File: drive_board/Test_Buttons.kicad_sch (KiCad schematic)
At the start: 0 parts

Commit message: New Stuff
- Reverse voltage protection
- D-Pad for test buttons
- Rotary encoder for test buttons
- Finished ethernet circuit
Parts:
- added D2, D3, D4, D5: Orange, symbol Device:LED
- added R2, R3, R4, R5: 1k, Resistor_SMD:R_0603_1608Metric_Pad0.98x0.95mm_HandSolder, symbol Device:R_US
- added S1: 94HBB08T, CoreBoard:DIPS762W56P254L991H597Q6N, symbol CoreBoard:94HBB08T
- added SW1, SW2, SW3, SW4: SW_Push, Button_Switch_SMD:SW_SPST_TL3305A, symbol Switch:SW_Push
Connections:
- new net: D3.1 (K), R3.2
- new net: D2.1 (K), R2.2
- new net: D5.1 (K), R5.2
- new net: D4.1 (K), R4.2
- new net +3.3V: D2.2 (A), D3.2 (A), D4.2 (A), D5.2 (A), S1.2 (C_1), S1.5 (C_2)
- new net Back: R5.1, SW4.2
- new net Forward: R2.1, SW1.2
- new net GND: SW1.1, SW2.1, SW3.1, SW4.1
- new net Left: R3.1, SW2.2
- new net RTRY1: S1.1
- new net RTRY2: S1.4 (2)
- new net RTRY4: S1.3 (4)
- new net Right: R4.1, SW3.2
- no-connect marks 0 -> 1
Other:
- note added: "D-Pad"
- note added: "Rotary Encoder"

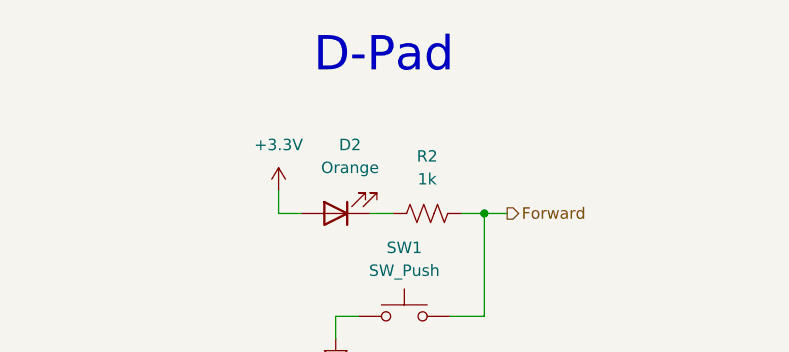
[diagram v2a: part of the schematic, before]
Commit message: More New Stuff
- Assigned pins on RoveNode
- Added some connectors
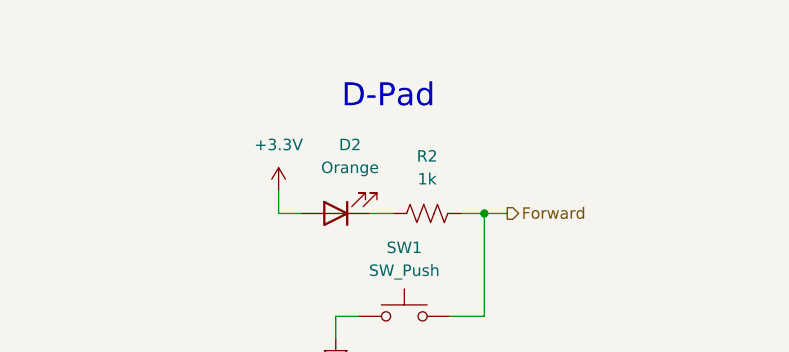
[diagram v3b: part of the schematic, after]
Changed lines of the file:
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@@
 	(text "D-Pad"
 		(exclude_from_sim no)
-		(at 76.454 23.114 0)
+		(at 76.962 27.686 0)
 		(effects
 			(font
-				(size 3.81 3.81)
+				(size 2.54 2.54)
 			)
 		)

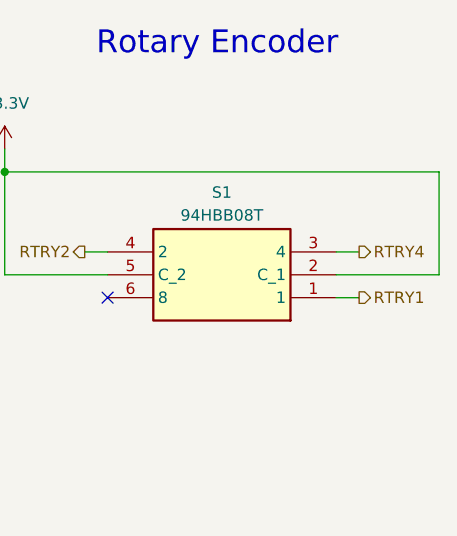
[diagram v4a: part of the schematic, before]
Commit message: Removed terminating resistors, assigned more pins, more connectors for CAN busses.
- Assigned GPIO inputs for test buttons and rotary encoder. Hopefully that works ._.
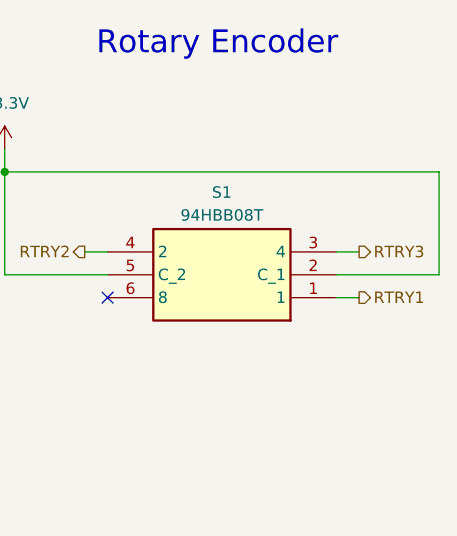
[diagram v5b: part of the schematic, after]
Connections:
- net RTRY4 renamed RTRY3
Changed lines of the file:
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@@
 		)
 	)
-	(hierarchical_label "RTRY4"
+	(hierarchical_label "RTRY3"
 		(shape output)
 		(at 193.04 50.8 0)

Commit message: Finish schematic
- Finished requirements
- Cleaned up and organized some stuff
- Can still clean up a little more
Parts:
- added D10, D11, D12, D13, D14, D7, D8, D9: Orange, symbol Device:LED
- added Q1, Q2, Q3, Q4, Q5, Q6, Q7, Q8: AO3401A, Package_TO_SOT_SMD:SOT-23, symbol Transistor_FET:AO3401A
- added R10, R11, R12, R13, R14, R7, R8, R9: 2.2k, symbol Device:R_US
- R3: renamed from R2; value 1k -> 2.2k
- R4: renamed from R3; value 1k -> 2.2k
- R5: renamed from R4; value 1k -> 2.2k
- R6: renamed from R5; value 1k -> 2.2k
- renumbered D2 to D3, D3 to D4, D4 to D5, D5 to D6
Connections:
- net +3.3V: now also Q1.2 (S), Q2.2 (S), Q3.2 (S), Q4.2 (S), Q5.2 (S), Q6.2 (S), Q7.2 (S), Q8.2 (S)
- net GND: now also D10.1 (K), D11.1 (K), D12.1 (K), D13.1 (K), D14.1 (K), D7.1 (K), D8.1 (K), D9.1 (K)
- net RTRY3 renamed RTRY4
- new net: D11.2 (A), R11.2
- new net: Q7.3 (D), R13.1
- new net: D13.2 (A), R13.2
- new net: D10.2 (A), R10.2
- new net: Q1.3 (D), R7.1
- new net: D7.2 (A), R7.2
- new net: D14.2 (A), R14.2
- new net: Q4.3 (D), R10.1
- new net: D12.2 (A), R12.2
- new net: Q3.3 (D), R9.1
- new net: Q6.3 (D), R12.1
- new net: Q2.3 (D), R8.1
- new net: D8.2 (A), R8.2
- new net: Q8.3 (D), R14.1
- new net: Q5.3 (D), R11.1
- new net: D9.2 (A), R9.2
- new net BLMOT_T: Q7.1 (G)
- new net BLMOT_W: Q5.1 (G)
- new net BRMOT_T: Q8.1 (G)
- new net BRMOT_W: Q6.1 (G)
- new net FLMOT_T: Q3.1 (G)
- new net FLMOT_W: Q1.1 (G)
- new net FRMOT_T: Q4.1 (G)
- new net FRMOT_W: Q2.1 (G)
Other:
- note added: "Motor Activation LEDs"
- moved on the sheet: D3, D4, D5, D6, R3, R4, R5, R6, S1, SW1, SW2, SW3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

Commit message: Organize schematic stuff
- Did new stuff lol!1! 67
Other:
- moved on the sheet: D10, D11, D12, D13, D14, D3, D4, D5, D6, D7, D8, D9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

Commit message: Adjust according to schematic review
- Added some pull down resistors and such
- Lowkey forgot because I forgot to commit and am a couple days late.
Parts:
- added R15, R16, R17, R18, R19, R20, R21, R22: 10k, symbol Device:R_US
- R10, R11, R12, R13, R14, R3, R4, R5, R6, R7, R8, R9: value 2.2k -> 1k
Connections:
- net BLMOT_T: now also R21.1
- net BLMOT_W: now also R19.1
- net BRMOT_T: now also R22.1
- net BRMOT_W: now also R20.1
- net FLMOT_T: now also R17.1
- net FLMOT_W: now also R15.1
- net FRMOT_T: now also R18.1
- net FRMOT_W: now also R16.1
- net GND: now also R15.2, R16.2, R17.2, R18.2, R19.2, R20.2, R21.2, R22.2
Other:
- note added: "Dip Switch"
- note removed: "Rotary Encoder"
- moved on the sheet: D10, D11, D12, D13, D14, D9, Q3, Q4, Q5, Q6, Q7, Q8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
